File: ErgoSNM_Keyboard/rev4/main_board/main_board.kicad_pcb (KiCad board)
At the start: 2 copper layers, 116.5 x 105 mm, 79 parts, among them J1 Conn_MouseSensor, J3 Conn_MouseSensor, J4 Conn_01x10, J5 Conn_02x10_Odd_Even, SW2 RESET, SW3 RESET

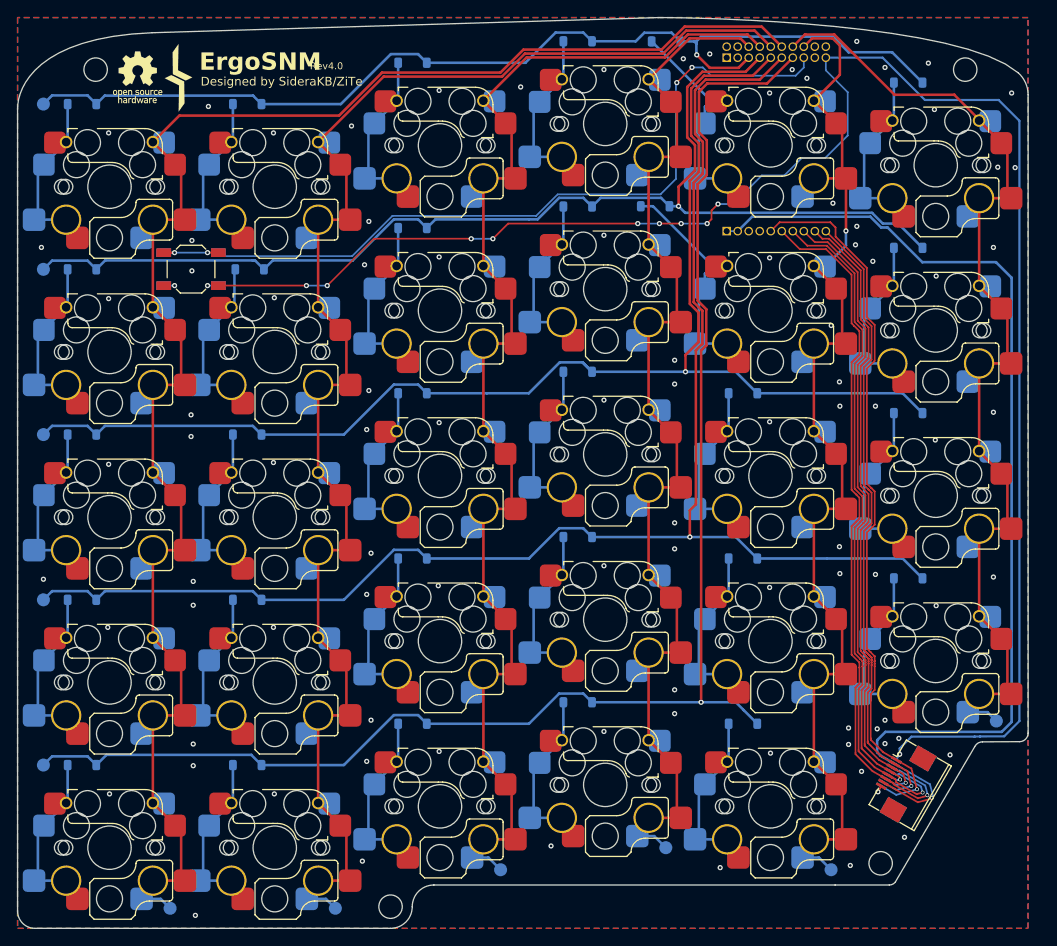
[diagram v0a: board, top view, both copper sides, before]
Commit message: feat: change pin header position
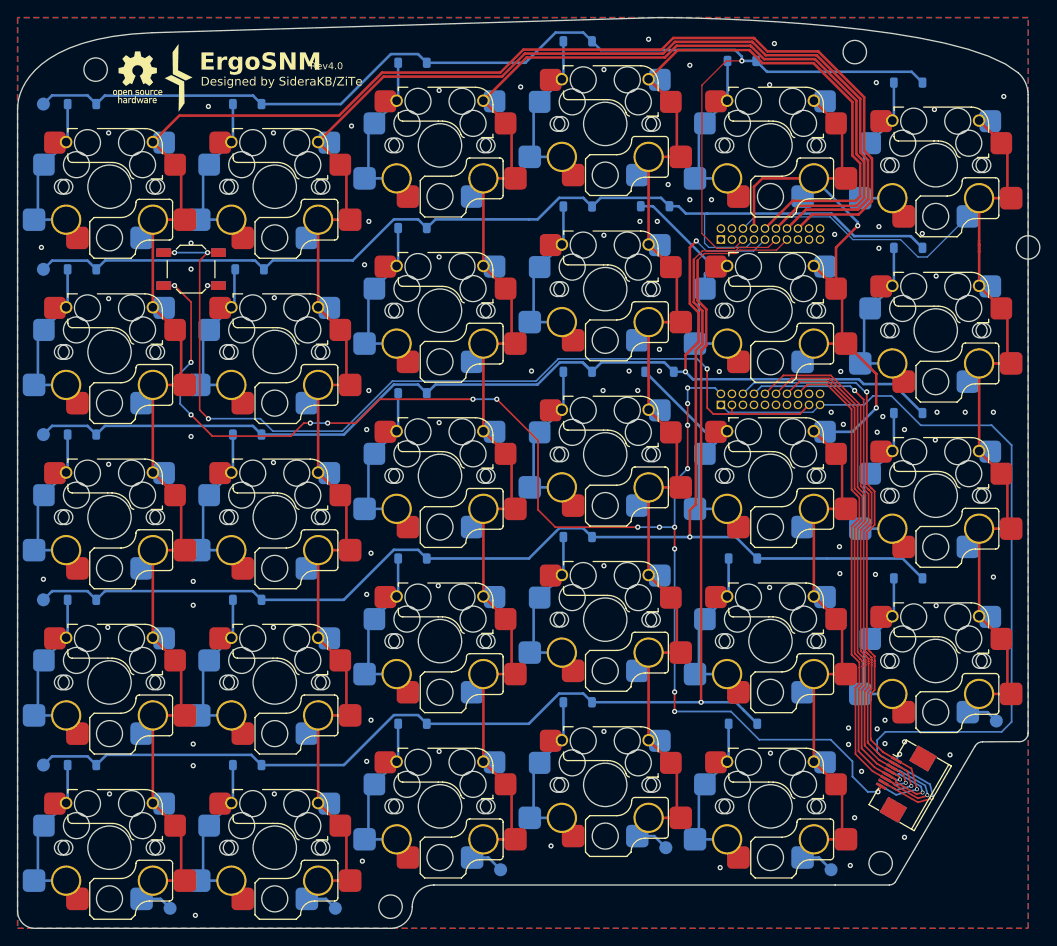
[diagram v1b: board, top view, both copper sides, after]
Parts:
- added H1: ~, MountingHole:MountingHole_2.7mm_M2.5_ISO14580, F.Cu at (207.5, 70.5)
- J4: value Conn_01x10 -> Conn_02x10_Odd_Even; footprint Connector_PinSocket_1.27mm:PinSocket_1x10_P1.27mm_Vertical -> Connector_PinSocket_1.27mm:PinSocket_2x10_P1.27mm_Vertical
- moved J5 21.0 mm to (172.1, 69.6)
- moved J4 20.0 mm to (172.1, 88.6)
- moved H8 12.9 mm to (187.5, 48.0)
- moved D17 9.94 mm to (165.0, 84.8)
- moved D5 9.03 mm to (174.5, 49.0)
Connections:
- J4 pad 10: MOTION -> SCLK
- J4 pad 2: VDD -> GND
- J4 pad 3: GND -> RESET
- J4 pad 4: GND -> unconnected-(J4-Pin_4-Pad4)
- J4 pad 5: IO_0 -> unconnected-(J4-Pin_5-Pad5)
- J4 pad 6: nCS -> IO_0
- J4 pad 7: MISO -> unconnected-(J4-Pin_7-Pad7)
- J4 pad 8: MOSI -> MOTION
- J4 pad 9: SCLK -> unconnected-(J4-Pin_9-Pad9)
- J5 pad 1: GND -> unconnected-(J5-Pin_1-Pad1)
- J5 pad 10: COL_1 -> COL_3
- J5 pad 12: COL_0 -> COL_2
- J5 pad 14: COL_5 -> COL_1
- J5 pad 15: RESET -> unconnected-(J5-Pin_15-Pad15)
- J5 pad 16: COL_4 -> COL_0
- J5 pad 19: GND -> unconnected-(J5-Pin_19-Pad19)
- J5 pad 2: GND -> unconnected-(J5-Pin_2-Pad2)
- J5 pad 20: GND -> unconnected-(J5-Pin_20-Pad20)
- J5 pad 6: COL_3 -> COL_5
- J5 pad 8: COL_2 -> COL_4
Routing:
- net GND: track 204.6 -> 160.4 mm, vias 107 -> 115
- net COL_3: track 129.0 -> 166.3 mm
- net COL_2: track 150.8 -> 186.6 mm
- net COL_1: track 173.3 -> 207.8 mm
- net COL_0: track 194.0 -> 227.0 mm
- net ROW_3: track 174.5 -> 153.1 mm
- net ROW_4: track 174.1 -> 152.7 mm
- net ROW_2: track 156.3 -> 137.4 mm, vias 1 -> 2
- net VDD: track 120.5 -> 101.8 mm
- net ROW_0: track 120.0 -> 138.6 mm
- net nCS: track 83.1 -> 64.5 mm
- net MISO: track 80.4 -> 64.5 mm
- net RESET: track 93.8 -> 108.8 mm
- net ROW_1: track 135.2 -> 120.5 mm, vias 1 -> 0
- net IO_0: track 83.5 -> 69.4 mm, vias 1 -> 2
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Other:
- outline, holes or cut-outs redrawn

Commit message: feat: update the connectors of the main board and core board
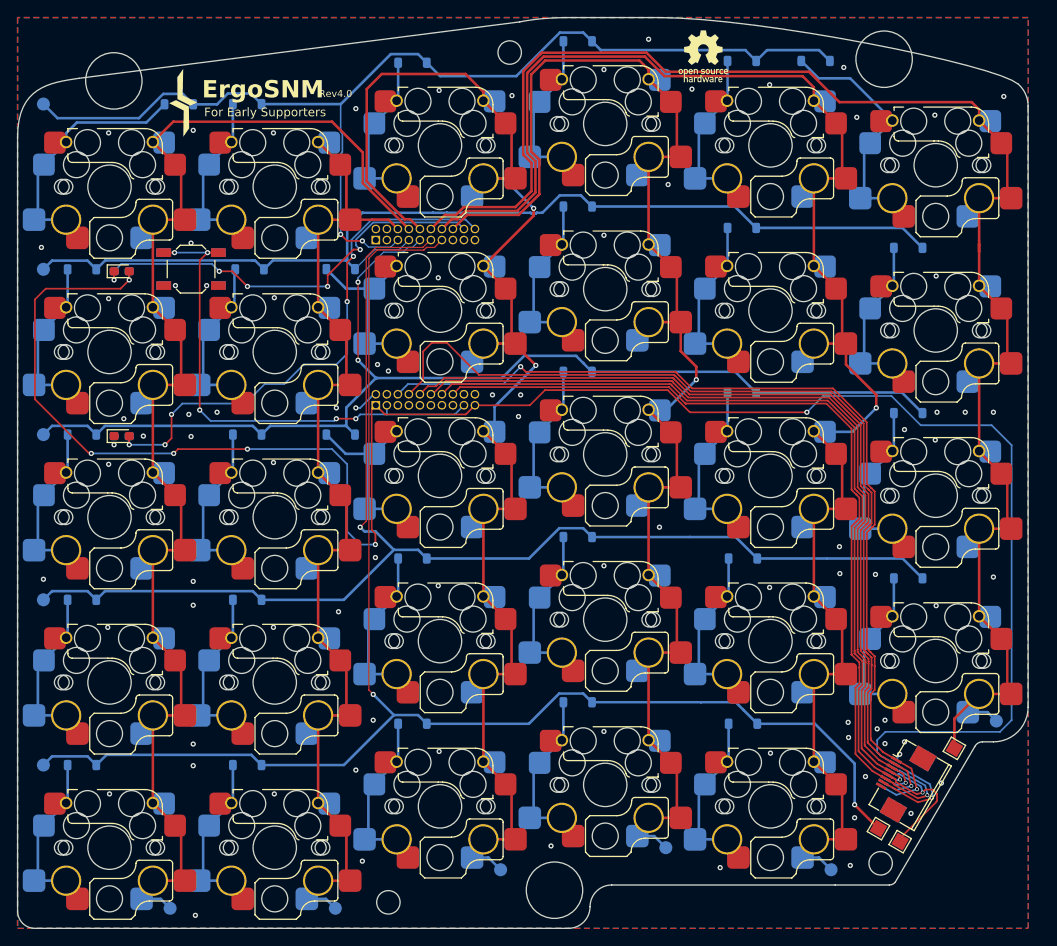
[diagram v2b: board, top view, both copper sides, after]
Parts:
- removed H9: ~, MountingHole:MountingHole_2.7mm_M2.5_ISO14580
- added H2: ~, ErgoSNM_Keyboard:mounting_hole_6.5mm, F.Cu at (190.9, 48.8)
- added H3: ~, ErgoSNM_Keyboard:mounting_hole_6.5mm, F.Cu at (152.9, 144.6)
- added LD1: LED, LED_SMD:LED_0603_1608Metric_Pad1.05x0.95mm_HandSolder, F.Cu at (103.0, 73.2)
- added LD2: LED, LED_SMD:LED_0603_1608Metric_Pad1.05x0.95mm_HandSolder, F.Cu at (103.0, 92.2)
- added LD3: LED, LED_SMD:LED_0603_1608Metric_Pad1.05x0.95mm_HandSolder, B.Cu at (103.0, 92.2)
- added LD4: LED, LED_SMD:LED_0603_1608Metric_Pad1.05x0.95mm_HandSolder, B.Cu at (103.0, 73.2)
- added TP12: TestPoint, TestPoint:TestPoint_Pad_1.5x1.5mm, F.Cu at (192.8, 139.0)
- added TP13: TestPoint, TestPoint:TestPoint_Pad_1.5x1.5mm, F.Cu at (199.0, 128.2)
- added TP14: TestPoint, TestPoint:TestPoint_Pad_1.5x1.5mm, F.Cu at (190.2, 137.5)
- H10, H8: moved to B.Cu
- H7: footprint MountingHole:MountingHole_2.7mm_M2.5_ISO14580 -> ErgoSNM_Keyboard:mounting_hole_6.5mm
- moved H1 105.5 mm to (133.8, 146.0)
- moved H8 39.8 mm to (147.7, 48.0), turned to 180 degrees
- moved J4 39.8 mm to (132.3, 88.7)
- moved J5 39.8 mm to (132.3, 69.6)
- moved D1 11.2 mm to (109.6, 54.0)
- moved D6 11.0 mm to (183.0, 49.0)
- moved D11 10.3 mm to (174.5, 68.2)
- moved D17 9.80 mm to (174.5, 87.2)
- moved D15 9.55 mm to (128.2, 92.1)
- moved D9 9.54 mm to (128.2, 73.0)
- moved H7 2.47 mm to (102.1, 51.3)
- turned H10 to 180 degrees
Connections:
- J5 pad 10: COL_3 -> COL_2
- J5 pad 12: COL_2 -> COL_5
- J5 pad 14: COL_1 -> COL_4
- J5 pad 16: COL_0 -> COL_3
- J5 pad 18: unconnected-(J5-Pin_18-Pad18) -> LED_CHG
- J5 pad 20: unconnected-(J5-Pin_20-Pad20) -> LED_STA
- J5 pad 6: COL_5 -> COL_1
- J5 pad 8: COL_4 -> COL_0
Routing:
- net GND: track 160.4 -> 3.70 mm, vias 115 -> 85
- net VDD: track 101.8 -> 236.6 mm, vias 1 -> 7
- net COL_1: track 207.8 -> 121.0 mm
- net COL_0: track 227.0 -> 152.7 mm
- net LED_STA: track 0.00 -> 62.3 mm, vias 0 -> 5
- net COL_5: track 122.1 -> 184.2 mm
- net LED_CHG: track 0.00 -> 49.3 mm, vias 0 -> 5
- net RESET: track 108.8 -> 60.1 mm, vias 4 -> 5
- net MISO: track 64.5 -> 112.0 mm
- net COL_4: track 138.9 -> 184.5 mm, vias 2 -> 1
- net MOTION: track 65.5 -> 109.7 mm, vias 2 -> 1
- net IO_0: track 69.4 -> 108.7 mm
- net MOSI: track 59.6 -> 97.9 mm
- net SCLK: track 63.1 -> 101.3 mm
- net nCS: track 64.5 -> 102.8 mm
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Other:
- outline, holes or cut-outs redrawn
- board text removed: "Designed by SideraKB/ZiTe"

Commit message: fix: add B5819 for battery reverse protection
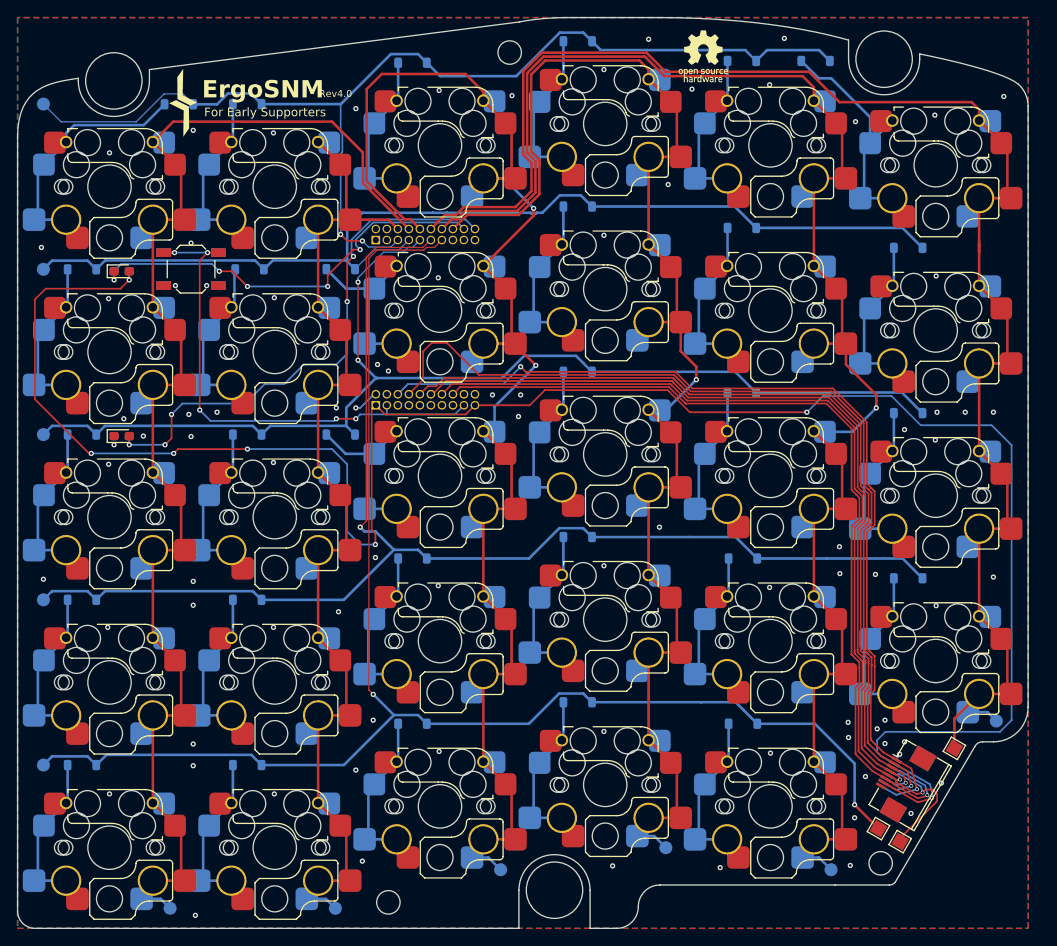
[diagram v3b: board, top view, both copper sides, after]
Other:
- outline, holes or cut-outs redrawn
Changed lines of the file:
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@@
 		(layer "F.SilkS")
 	)
+	(gr_line
+		(start 97.998781 51.3)
+		(end 98.008931 51)
+		(stroke
+			(width 0.05)
+			(type default)
+		)
+		(layer "Edge.Cuts")
+	)
 	(gr_arc
 		(start 93 149)
@@
 		(layer "Edge.Cuts")
 	)
+	(gr_line
+		(start 148.798781 144.6)
+		(end 148.798781 149)
+		(stroke
+			(width 0.05)
+			(type default)
+		)
+		(layer "Edge.Cuts")
+	)
+	(gr_arc
+		(start 162.56 146.5)
+		(mid 163.292233 144.732233)
+		(end 165.06 144)
+		(stroke
+			(width 0.05)
+			(type default)
+		)
+		(layer "Edge.Cuts")
+	)
 	(gr_arc
-		(start 157 146.5)
-		(mid 157.732233 144.732233)
-		(end 159.5 144)
+		(start 106.201219 51.3)
+		(mid 102.1 55.401219)
+		(end 97.998781 51.3)
 		(stroke
 			(width 0.05)
@@
 	)
 	(gr_line
-		(start 98.1 51)
+		(start 106.201219 50)
 		(end 148.9 44.5)
 		(stroke
@@
 		(layer "Edge.Cuts")
 	)
+	(gr_arc
+		(start 195.001219 48.8)
+		(mid 190.9 52.901219)
+		(end 186.798781 48.8)
+		(stroke
+			(width 0.05)
+			(type default)
+		)
+		(layer "Edge.Cuts")
+	)
 	(gr_line
 		(start 185.25 144)
-		(end 159.5 144)
+		(end 165.06 144)
+		(stroke
+			(width 0.05)
+			(type default)
+		)
+		(layer "Edge.Cuts")
+	)
+	(gr_line
+		(start 157.001219 144.6)
+		(end 157 149)
 		(stroke
 			(width 0.05)
@@
 		(layer "Edge.Cuts")
 	)
+	(gr_line
+		(start 186.798781 48.8)
+		(end 186.8 46.6)
+		(stroke
+			(width 0.05)
+			(type default)
+		)
+		(layer "Edge.Cuts")
+	)
 	(gr_arc
-		(start 157 146.5)
-		(mid 156.267767 148.267767)
-		(end 154.5 149)
+		(start 162.56 146.5)
+		(mid 161.827767 148.267767)
+		(end 160.06 149)
 		(stroke
 			(width 0.05)
@@
 	(gr_line
 		(start 93 149)
-		(end 154.5 149)
+		(end 148.798781 149)
 		(stroke
 			(width 0.05)
@@
 	(gr_curve
 		(pts
-			(xy 164.9 44) (xy 176.6 44) (xy 203.8 49.4) (xy 206.378979 51.683389)
+			(xy 164.9 44) (xy 176.6 44) (xy 184 45.8) (xy 186.8 46.6)
 		)
 		(stroke
@@
 	(gr_curve
 		(pts
-			(xy 98.1 51) (xy 94.7 51.5) (xy 91 52) (xy 91 57.8)
+			(xy 98.008931 51) (xy 94.7 51.5) (xy 91 52) (xy 91 57.8)
 		)
 		(stroke
@@
 		(layer "Edge.Cuts")
 	)
+	(gr_line
+		(start 195.001219 48.8)
+		(end 195.001219 48.2)
+		(stroke
+			(width 0.05)
+			(type default)
+		)
+		(layer "Edge.Cuts")
+	)
+	(gr_line
+		(start 106.201219 51.3)
+		(end 106.201219 50)
+		(stroke
+			(width 0.05)
+			(type default)
+		)
+		(layer "Edge.Cuts")
+	)
+	(gr_curve
+		(pts
+			(xy 206.378979 51.683387) (xy 204.4 50) (xy 195.001219 48.2) (xy 195.001219 48.2)
+		)
+		(stroke
+			(width 0.05)
+			(type default)
+		)
+		(layer "Edge.Cuts")
+	)
 	(gr_curve
 		(pts
@@
 	)
 	(gr_line
+		(start 160.06 149)
+		(end 157 149)
+		(stroke
+			(width 0.05)
+			(type default)
+		)
+		(layer "Edge.Cuts")
+	)
+	(gr_line
 		(start 201.348368 128.052786)
 		(end 192.207107 143.633974)
@@
 		(layer "Edge.Cuts")
 	)
+	(gr_arc
+		(start 148.798781 144.6)
+		(mid 152.9 140.498781)
+		(end 157.001219 144.6)
+		(stroke
+			(width 0.05)
+			(type default)
+		)
+		(layer "Edge.Cuts")
+	)
 	(gr_line
 		(start 203.5 127.5)
@@
 	)
 	(via
-		(at 187.75 55.5)
+		(at 187.6 56)
 		(size 0.6)
 		(drill 0.3)
@@
 	)
 	(via
-		(at 152.5 139.5)
+		(at 159.6 141.8)
 		(size 0.6)
 		(drill 0.3)
@@
 	)
 	(via
-		(at 186.25 49.75)
+		(at 179.4 46.4)
 		(size 0.6)
 		(drill 0.3)
@@
 	)
 	(via
-		(at 101.5 57.3)
+		(at 101.6 59.6)
 		(size 0.6)
 		(drill 0.3)
@@
 	)
 	(segment
-		(start 97.824696 56.1)
-		(end 96.6 57.324696)
-		(width 0.3)
-		(layer "B.Cu")
-		(net 3)
-	)
-	(segment
 		(start 93.345 61.655)
 		(end 93.345 66.855)
@@
 	)
 	(segment
-		(start 107.95 54)
-		(end 105.85 56.1)
+		(start 96.6 57.324696)
+		(end 96.6 58.35)
 		(width 0.3)
 		(layer "B.Cu")
@@
 	)
 	(segment
-		(start 105.85 56.1)
-		(end 97.824696 56.1)
+		(start 96.6 58.4)
+		(end 94.04 60.96)
 		(width 0.3)
+		(locked yes)
 		(layer "B.Cu")
 		(net 3)
 	)
 	(segment
-		(start 96.6 58.4)
-		(end 94.04 60.96)
+		(start 97.524696 56.4)
+		(end 96.6 57.324696)
 		(width 0.3)
-		(locked yes)
 		(layer "B.Cu")
 		(net 3)
 	)
 	(segment
-		(start 96.6 57.324696)
-		(end 96.6 58.35)
+		(start 107.95 54)
+		(end 105.55 56.4)
 		(width 0.3)
 		(layer "B.Cu")
@@
 	)
 	(segment
+		(start 105.55 56.4)
+		(end 97.524696 56.4)
+		(width 0.3)
+		(layer "B.Cu")
+		(net 3)
+	)
+	(segment
 		(start 94.04 60.96)
 		(end 93.345 61.655)
@@
 	)
 	(segment
+		(start 104.681956 56.024)
+		(end 96.029 56.024)
+		(width 0.15)
+		(layer "B.Cu")
+		(net 4)
+	)
+	(segment
 		(start 128.441 59.513346)
 		(end 128.441 57.326654)
@@
 	)
 	(segment
+		(start 110.05 52.8)
+		(end 107.905956 52.8)
+		(width 0.15)
+		(layer "B.Cu")
+		(net 4)
+	)
+	(segment
 		(start 174.9 47.75)
 		(end 176.15 49)
@@
 	)
 	(segment
+		(start 111.25 54)
+		(end 110.05 52.8)
+		(width 0.15)
+		(layer "B.Cu")
+		(net 4)
+	)
+	(segment
 		(start 137.174 48.211)
 		(end 134.034 48.211)
@@
 	)
 	(segment
+		(start 96.029 56.024)
+		(end 93.98 53.975)
+		(width 0.15)
+		(layer "B.Cu")
+		(net 4)
+	)
+	(segment
+		(start 107.905956 52.8)
+		(end 104.681956 56.024)
+		(width 0.15)
+		(layer "B.Cu")
+		(net 4)
+	)
+	(segment
 		(start 157.225 46.735)
 		(end 156.224 45.734)
@@
 	)
 	(segment
-		(start 107.79989 52.8)
-		(end 110.05 52.8)
-		(width 0.3)
-		(layer "B.Cu")
-		(net 4)
-	)
-	(segment
 		(start 128.25 53.995)
 		(end 128.27 53.975)
@@
 	)
 	(segment
-		(start 104.99989 55.6)
-		(end 107.79989 52.8)
-		(width 0.3)
-		(layer "B.Cu")
-		(net 4)
-	)
-	(segment
-		(start 95.605 55.6)
-		(end 104.99989 55.6)
-		(width 0.3)
-		(layer "B.Cu")
-		(net 4)
-	)
-	(segment
 		(start 157.225 46.735)
 		(end 158.24 47.75)
@@
 	)
 	(segment
-		(start 110.05 52.8)
-		(end 111.25 54)
-		(width 0.3)
-		(layer "B.Cu")
-		(net 4)
-	)
-	(segment
 		(start 134.034 48.211)
 		(end 128.27 53.975)
@@
 	)
 	(segment
-		(start 93.98 53.975)
-		(end 95.605 55.6)
-		(width 0.3)
-		(layer "B.Cu")
-		(net 4)
-	)
-	(segment
 		(start 128.25 57.135654)
 		(end 128.25 53.995)
@@
 	)
 	(segment
-		(start 186.977 51)
-		(end 191.85 55.873)
-		(width 0.3)
-		(layer "B.Cu")
-		(net 9)
-	)
-	(segment
 		(start 188.595 59.178)
 		(end 188.595 64.378)
@@
 	)
 	(segment
-		(start 181.35 49)
-		(end 183.35 51)
+		(start 189.29 55.49)
+		(end 189.29 58.483)
 		(width 0.3)
 		(layer "B.Cu")
@@
 	)
 	(segment
+		(start 183.35 51)
+		(end 184.8 51)
+		(width 0.3)
+		(layer "B.Cu")
+		(net 9)
+	)
+	(segment
 		(start 189.29 58.433)
 		(end 189.29 58.483)
@@
 	)
 	(segment
-		(start 191.85 64.823)
-		(end 188.15 64.823)
+		(start 184.8 51)
+		(end 189.29 55.49)
 		(width 0.3)
-		(locked yes)
 		(layer "B.Cu")
 		(net 9)
 	)
 	(segment
-		(start 183.35 51)
-		(end 186.977 51)
+		(start 191.85 64.823)
+		(end 188.15 64.823)
 		(width 0.3)
+		(locked yes)
 		(layer "B.Cu")
 		(net 9)
@@
 	)
 	(segment
+		(start 181.35 49)
+		(end 183.35 51)
+		(width 0.3)
+		(layer "B.Cu")
+		(net 9)
+	)
+	(segment
 		(start 130.75 66.5)
 		(end 138.917006 66.5)
@@
 		(members "03402e1c-4196-406a-9c8e-516fa9ebe30d" "05a37bf4-4d4b-4212-84f1-5b849a7567d6"
 			"0e43d0d2-b98a-4044-af56-156abc2ae2c2" "2230d249-4157-4c23-a5b5-bfecff002015"
-			"2be2f41f-d6e4-41e5-a23e-76cf77062d4b" "33b7d69e-802e-447e-8680-3becd3cda47d"
-			"385e5bfe-8242-4a70-aeff-bb7f10a00332" "38ef71b5-c6a1-4e3d-833f-6c07ce5fc16c"
-			"39dd9ce9-b31e-4d82-bc94-f6eef0986a83" "3cf812ba-8998-4c20-8f65-b8c5ae276dde"
-			"45e22461-f706-4e29-83fb-4aef613e2c4e" "4b5318ff-44fc-406f-8a7c-16e4b5b9fc56"
+			"2be2f41f-d6e4-41e5-a23e-76cf77062d4b" "31833314-3558-491e-bfdf-a2a914a7f42f"
+			"33b7d69e-802e-447e-8680-3becd3cda47d" "385e5bfe-8242-4a70-aeff-bb7f10a00332"
+			"38ef71b5-c6a1-4e3d-833f-6c07ce5fc16c" "39dd9ce9-b31e-4d82-bc94-f6eef0986a83"
+			"3cf812ba-8998-4c20-8f65-b8c5ae276dde" "45e22461-f706-4e29-83fb-4aef613e2c4e"
+			"48d9f66a-9c4c-45e3-a1a1-f694349f655b" "4b5318ff-44fc-406f-8a7c-16e4b5b9fc56"
 			"52fd2cb0-b8f0-4956-92f1-fea259b182de" "5751b17b-e2f2-4feb-a273-8340efd37953"
 			"5d174ffa-c8fc-4361-a19b-377c7e9c7714" "6775ab95-3d5e-46ce-822a-40484e1714fb"
@@
 			"b53df87b-2750-4c2b-be19-85f413611116" "c12d8c58-2904-4283-a957-8462ec342aad"
 			"d275184e-9afc-45aa-be22-c4451f8d3821" "d9e4d402-60d9-4ecb-bdd8-08ae194bb7ab"
-			"e13b64da-f13e-430e-b55e-37263a5695ab" "e3179a29-d8df-4bda-a902-b3857e589dc4"
-			"e8400cb8-6954-4dfa-8634-5a6300f683a9" "e92ca759-ae0d-4e29-a9fc-2414f3bfa9f9"
-			"e93b32e4-bf37-47a6-a36b-ec230f28e0c9" "eb10ae7c-1e03-4487-aee8-ea4da237aba6"
-			"ed07ebe9-2d7a-44bb-8d2b-cbd65d011e06" "f040c093-53d3-4185-98b1-4b37e4ed84ec"
+			"db13fccd-68b4-4d00-9f58-83c28b143cb6" "e13b64da-f13e-430e-b55e-37263a5695ab"
+			"e3179a29-d8df-4bda-a902-b3857e589dc4" "e8400cb8-6954-4dfa-8634-5a6300f683a9"
+			"e92ca759-ae0d-4e29-a9fc-2414f3bfa9f9" "e93b32e4-bf37-47a6-a36b-ec230f28e0c9"
+			"eb10ae7c-1e03-4487-aee8-ea4da237aba6" "ed07ebe9-2d7a-44bb-8d2b-cbd65d011e06"
+			"ef1121c3-2f07-4ba1-806b-127d1b95e00a" "f040c093-53d3-4185-98b1-4b37e4ed84ec"
 			"f07e1092-e0e1-41e6-a615-05cc419f3a2e" "fa95f210-1a12-4d50-9442-da8972249d4d"
 			"fe405a90-c22d-4e78-87f2-1b2dcc91bc10"
